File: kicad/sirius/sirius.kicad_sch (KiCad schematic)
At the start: 58 parts, among them J1 IPEX_MHF1, J2 Power In, J3 Screw_Terminal, Q1 Q_PMOS_GSD, Q2 Q_NMOS_GSD, Q3 Q_NMOS_GSD, U1 Power_Connector, U2 AP63301WU-7, U3 RFM95W-915S2, U4 LC29H (DA), U5 Pi Zero 2W

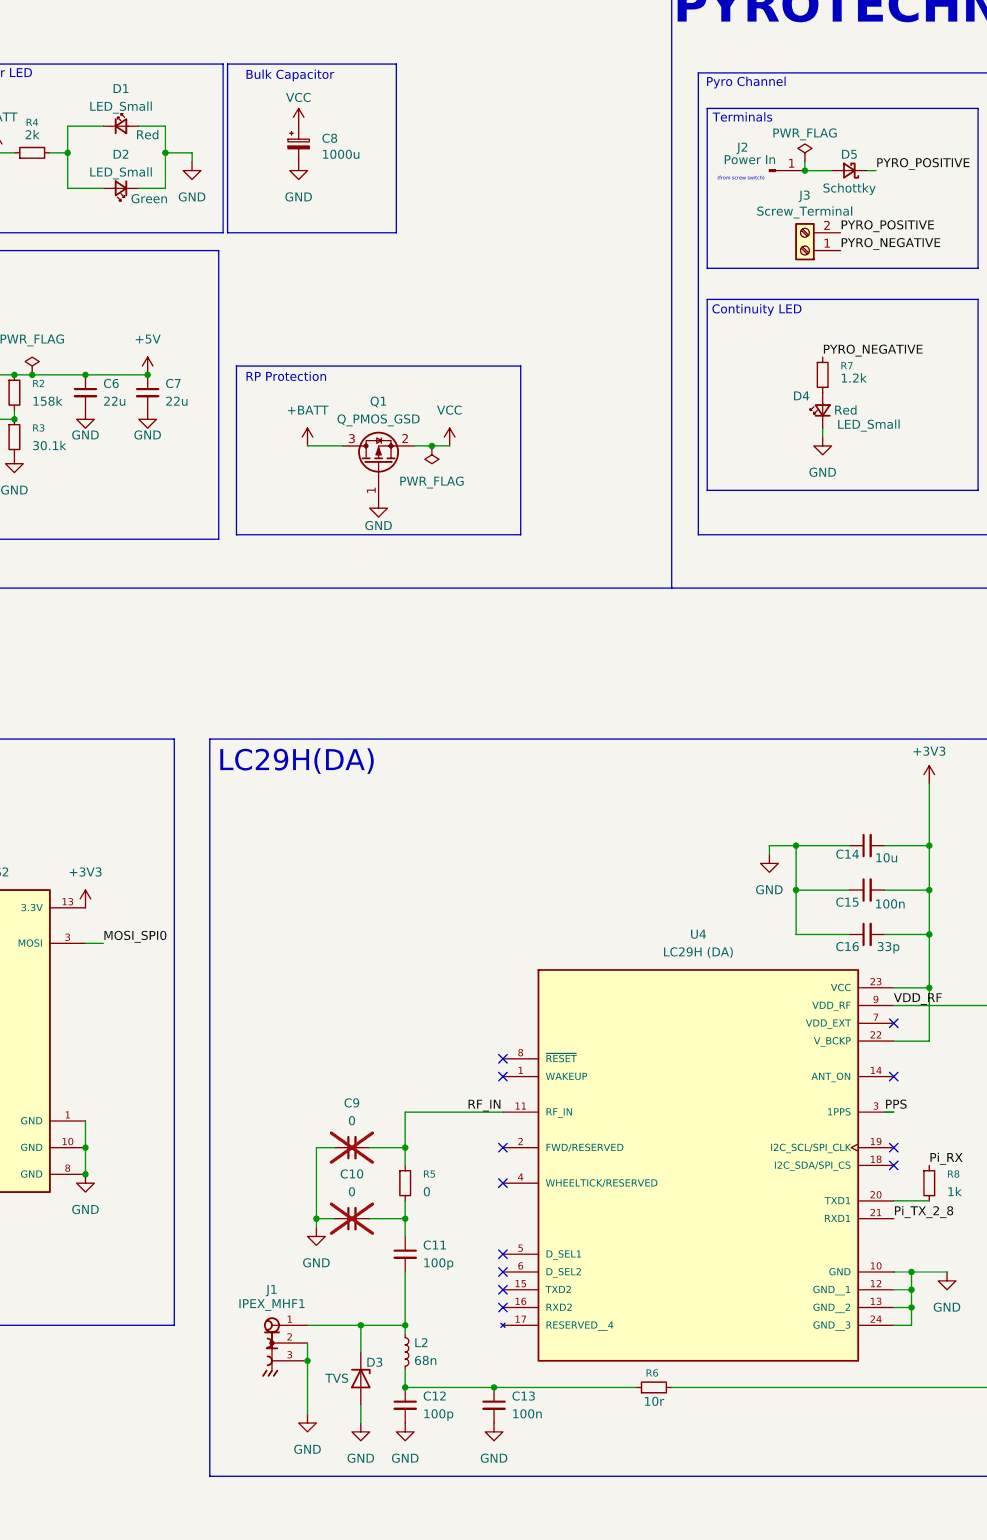
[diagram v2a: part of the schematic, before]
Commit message: Replace footprint of u.fl connector & screw terminal
Redesign board to accomodate larger footprint, make Sopdet a little smaller to qualify for $2 jlcpcb price, assign Digikey PN to all components, add a script which combines the BOM's of both boards so Digikey can more accurately detect cost savings
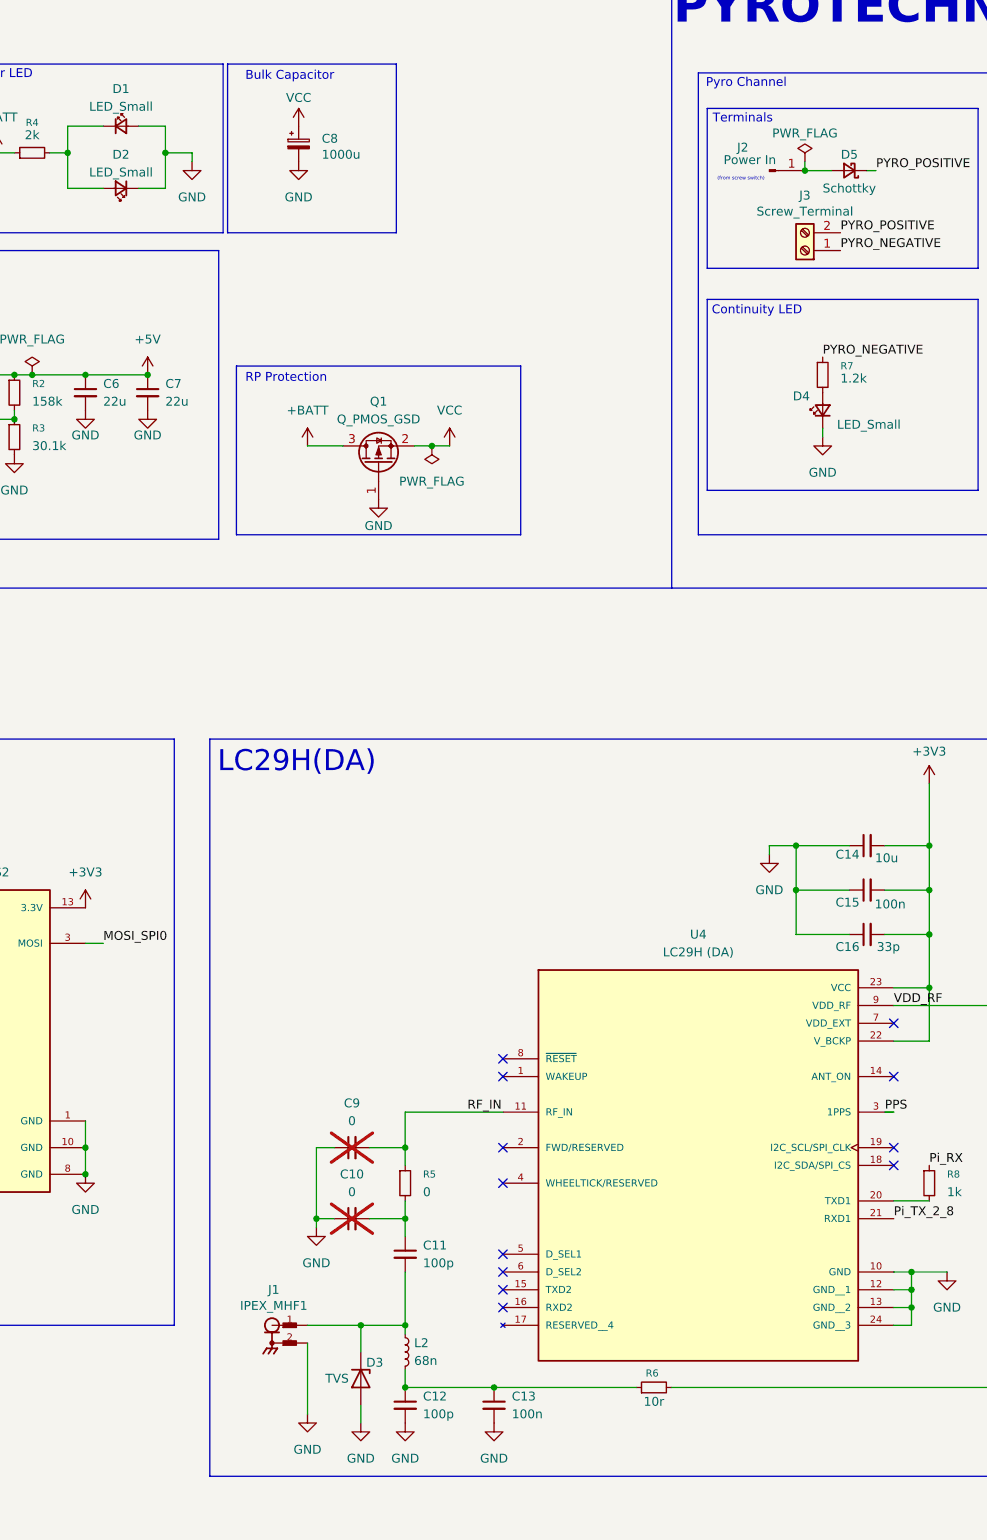
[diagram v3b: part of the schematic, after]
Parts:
- C1, C14: Digikey PN (none) -> 587-3258-1-ND
- C11, C12: Digikey PN (none) -> 490-1427-1-ND
- C13, C15, C4: Digikey PN (none) -> 399-C0603C104K3RACTUCT-ND
- C16: Digikey PN (none) -> 1276-1070-1-ND
- C5: Digikey PN (none) -> 1276-1037-1-ND
- C6, C7: Digikey PN (none) -> 587-3246-1-ND
- C8: Digikey PN (none) -> 565-HHXJ160ARA102MJC5GCT-ND
- D1, D4: Color Red -> (none)
- D10: Digikey PN (none) -> 1N4148WSRRGCT-ND
- D2: Color Green -> (none)
- J1: footprint sirius:ipex_mhf1 -> sirius:TE_CONMHF1-SMD-T; symbol sirius:IPEX_MHF1 -> sirius:CONMHF1-SMD-T; Digikey PN (none) -> 343-CONMHF1-SMD-TCT-ND
- J3: footprint TerminalBlock_Phoenix:TerminalBlock_Phoenix_MPT-0,5-2-2.54_1x02_P2.54mm_Horizontal -> sirius:CUI_TB002-500-02BE; Digikey PN (none) -> 102-6145-ND
- L2: Digikey PN (none) -> 490-1178-1-ND
- Q2, Q3: Digikey PN IRLML2502TRPBFCT-ND -> 31-DMN2058U-13CT-ND
- R1, R5: Digikey PN (none) -> 311-0.0GRCT-ND
- R10: Digikey PN (none) -> 311-100HRCT-ND
- R11: Digikey PN (none) -> 311-5.60KHRCT-ND
- R12, R14, R15, R16, R8: Digikey PN (none) -> RMCF0603FT1K00CT-ND
- R13: Digikey PN (none) -> 311-10.0KHRCT-ND
- R17: Digikey PN (none) -> A129679CT-ND
- R2: Digikey PN (none) -> 311-158KHRCT-ND
- R3: Digikey PN (none) -> RMCF0603FT30K1CT-ND
- R6: Digikey PN (none) -> RMCF0603FT10R0CT-ND
- R7: Digikey PN (none) -> 311-1.20KHRCT-ND
- R9: Digikey PN (none) -> 311-3.30KHRCT-ND
- U3: AVAILABILITY Unavailable -> (none); Availability In Stock -> (none); Check_prices https://www.snapeda.com/parts/RFM95W-915S2/RF/view-part/?re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 -> (none); Description_1 802.15.4 LoRa™ Transceiver Module 915MHz Antenna Not Includ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 -> (none); MF RF Solutions -> (none); MP RFM95W-915S2 -> (none); PACKAGE SMD-16 RF Solutions -> (none); PRICE None -> (none); Package Non Standard RF Solutions -> (none); Price None -> (none); STANDARD Manufacturer recommendations -> (none); SnapEDA_Link https://www.snapeda.com/parts/RFM95W-915S2/RF/view-part/?re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 -> (none)
- U4: Digikey PN (none) -> 2958-LC29HDAMDCT-ND
- U5: Availability In Stock -> (none); Check_prices https://www.snapeda.com/parts/RASPBERRY%20PI%20ZERO%202%20W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 -> (none); Description_1 At the heart of Raspberry Pi Zero 2 W is RP3A0, a custom-bu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 -> (none); MANUFACTURER Raspberry Pi -> (none); MF Raspberry Pi -> (none); MP RASPBERRY PI ZERO 2 W -> (none); PARTREV April 2024 -> (none); Package None -> (none); Price None -> (none); STANDARD Manufacturer Recommendations -> (none); SnapEDA_Link https://www.snapeda.com/parts/RASPBERRY%20PI%20ZERO%202%20W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 -> (none)
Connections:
- net GND: now also J1.4
